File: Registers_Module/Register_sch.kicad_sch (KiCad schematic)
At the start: 22 parts, among them U12 74LS245, U13 74LS173, U14 74LS173

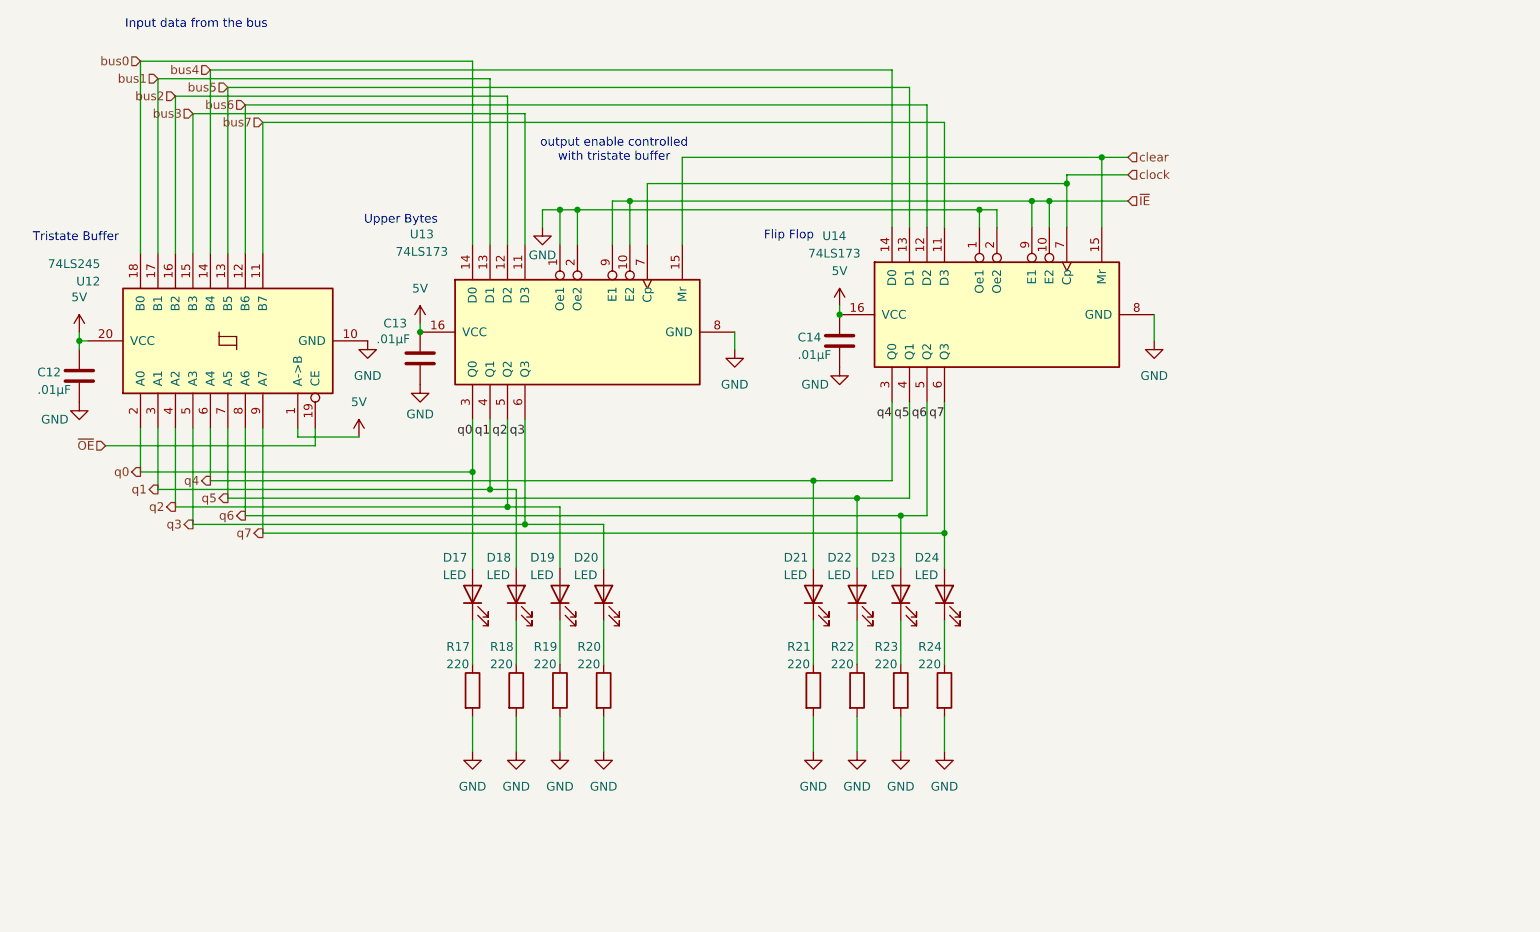
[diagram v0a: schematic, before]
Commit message: updated registers and alu
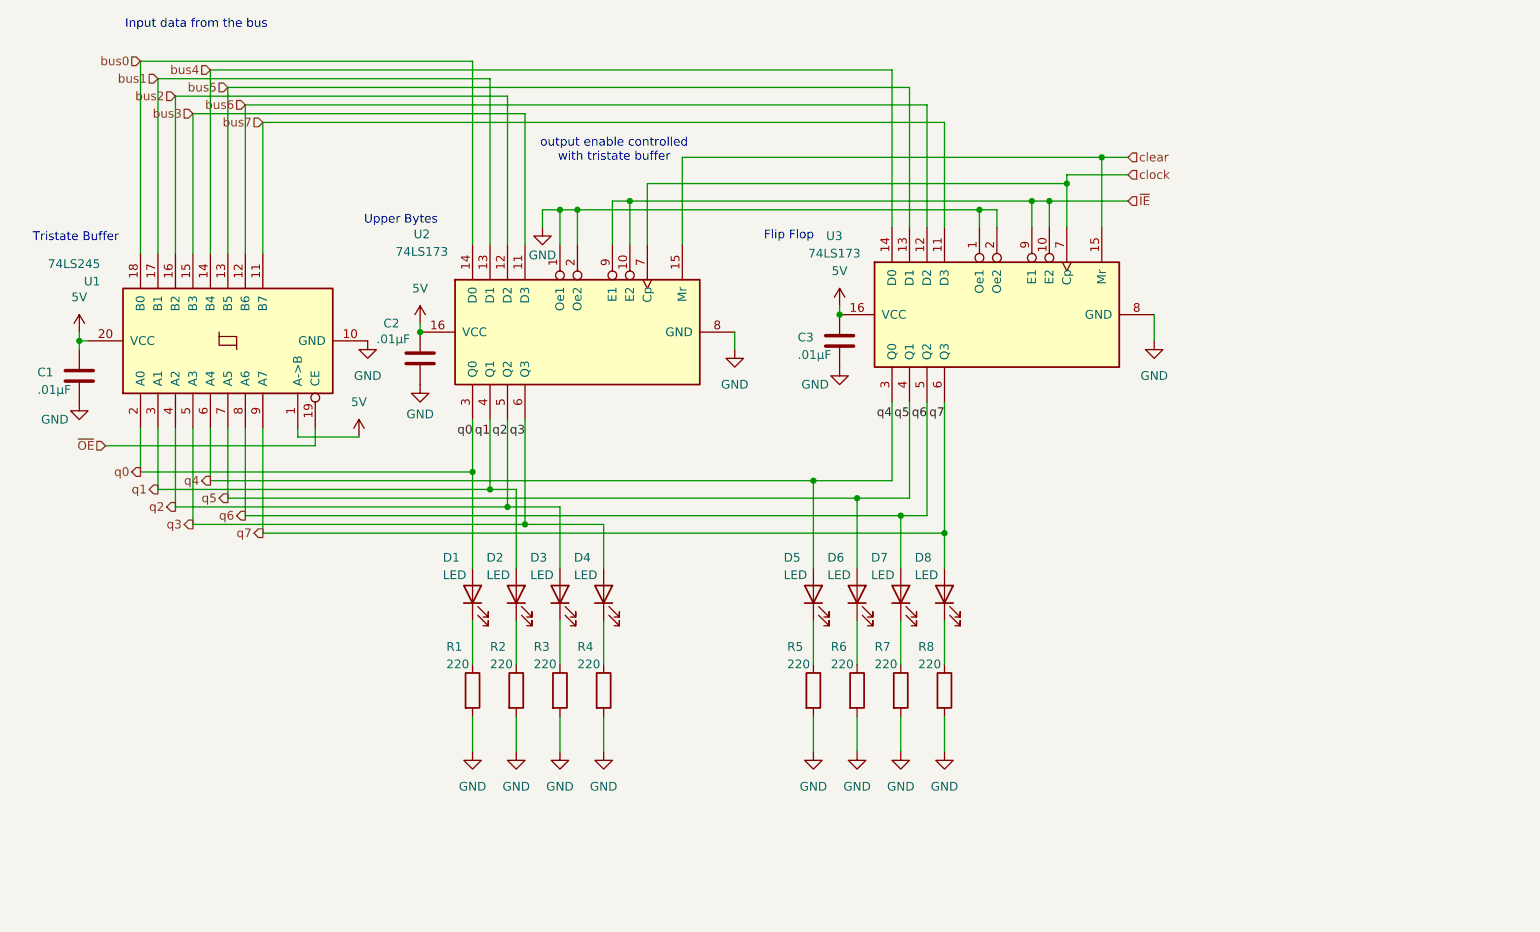
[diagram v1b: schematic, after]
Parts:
- renumbered C12 to C1, C13 to C2, C14 to C3, D17 to D1, D18 to D2, D19 to D3, D20 to D4, D21 to D5, D22 to D6, D23 to D7, D24 to D8, R17 to R1, R18 to R2, R19 to R3, R20 to R4, R21 to R5, R22 to R6, R23 to R7, R24 to R8, U12 to U1, U13 to U2, U14 to U3

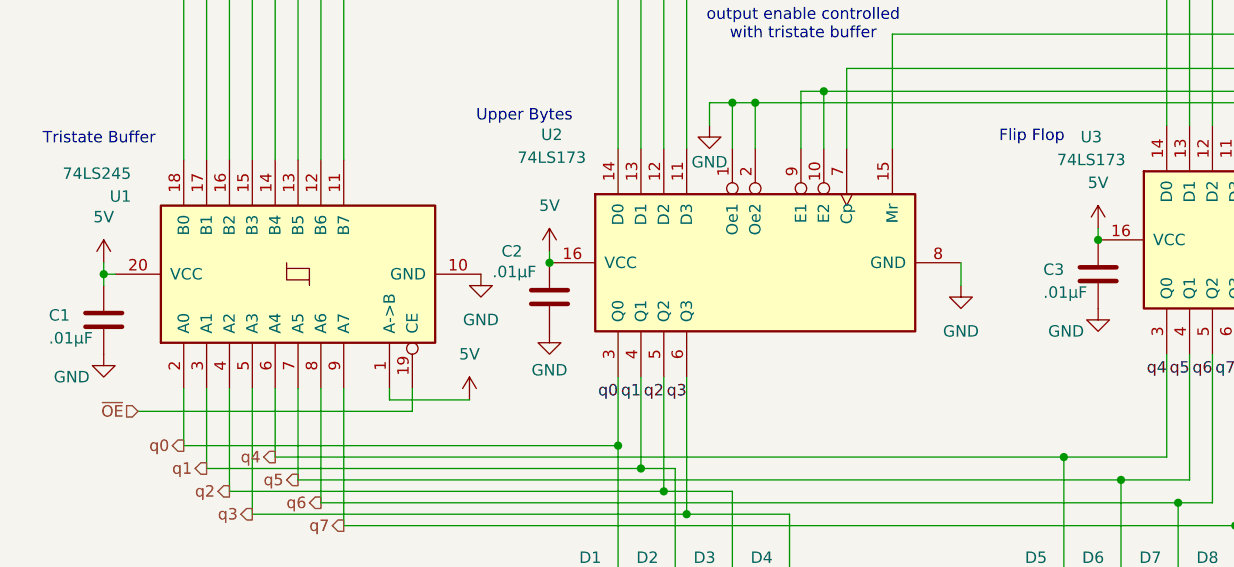
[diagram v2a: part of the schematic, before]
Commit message: added cap's between power pins
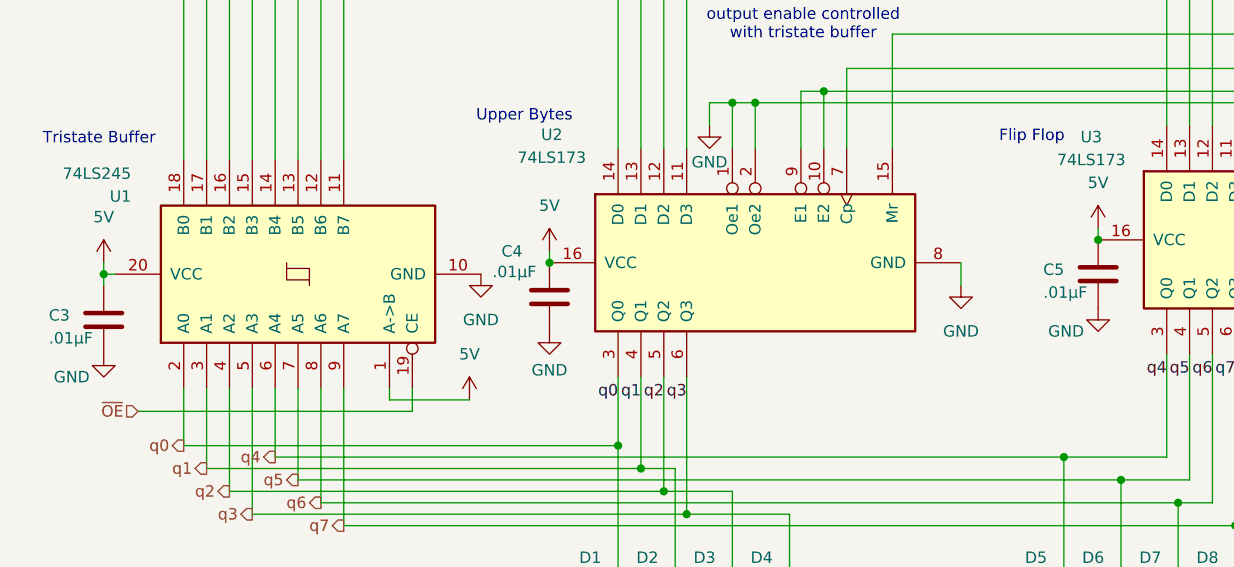
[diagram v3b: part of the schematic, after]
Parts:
- renumbered C1 to C3, C2 to C4, C3 to C5

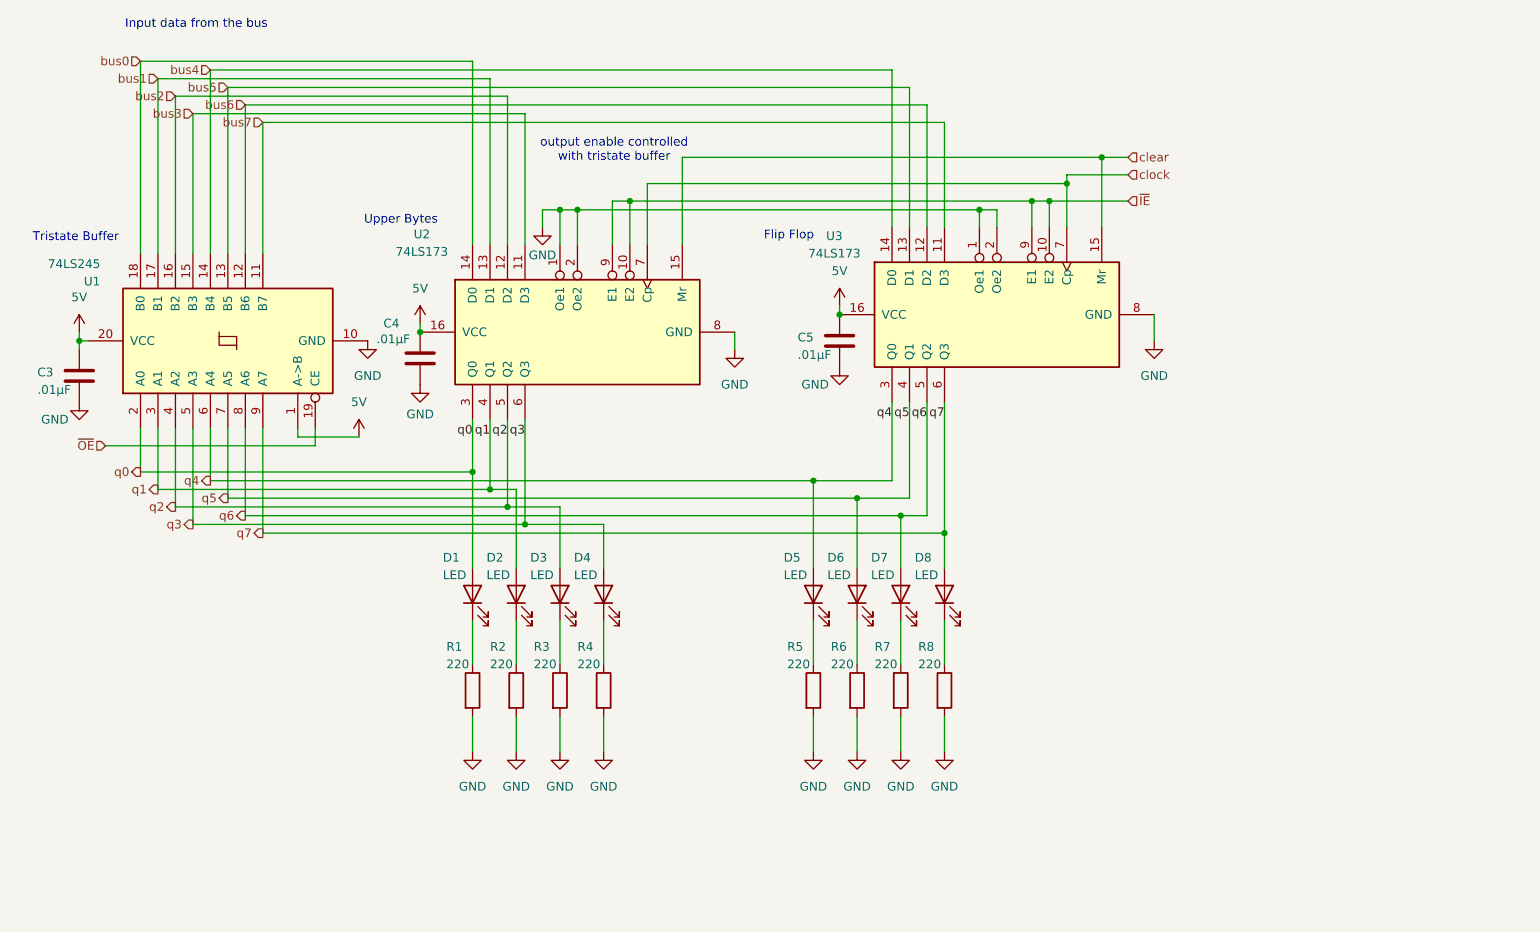
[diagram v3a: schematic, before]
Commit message: updated RAM, changed bus alignment in ALU, RAM, and registers
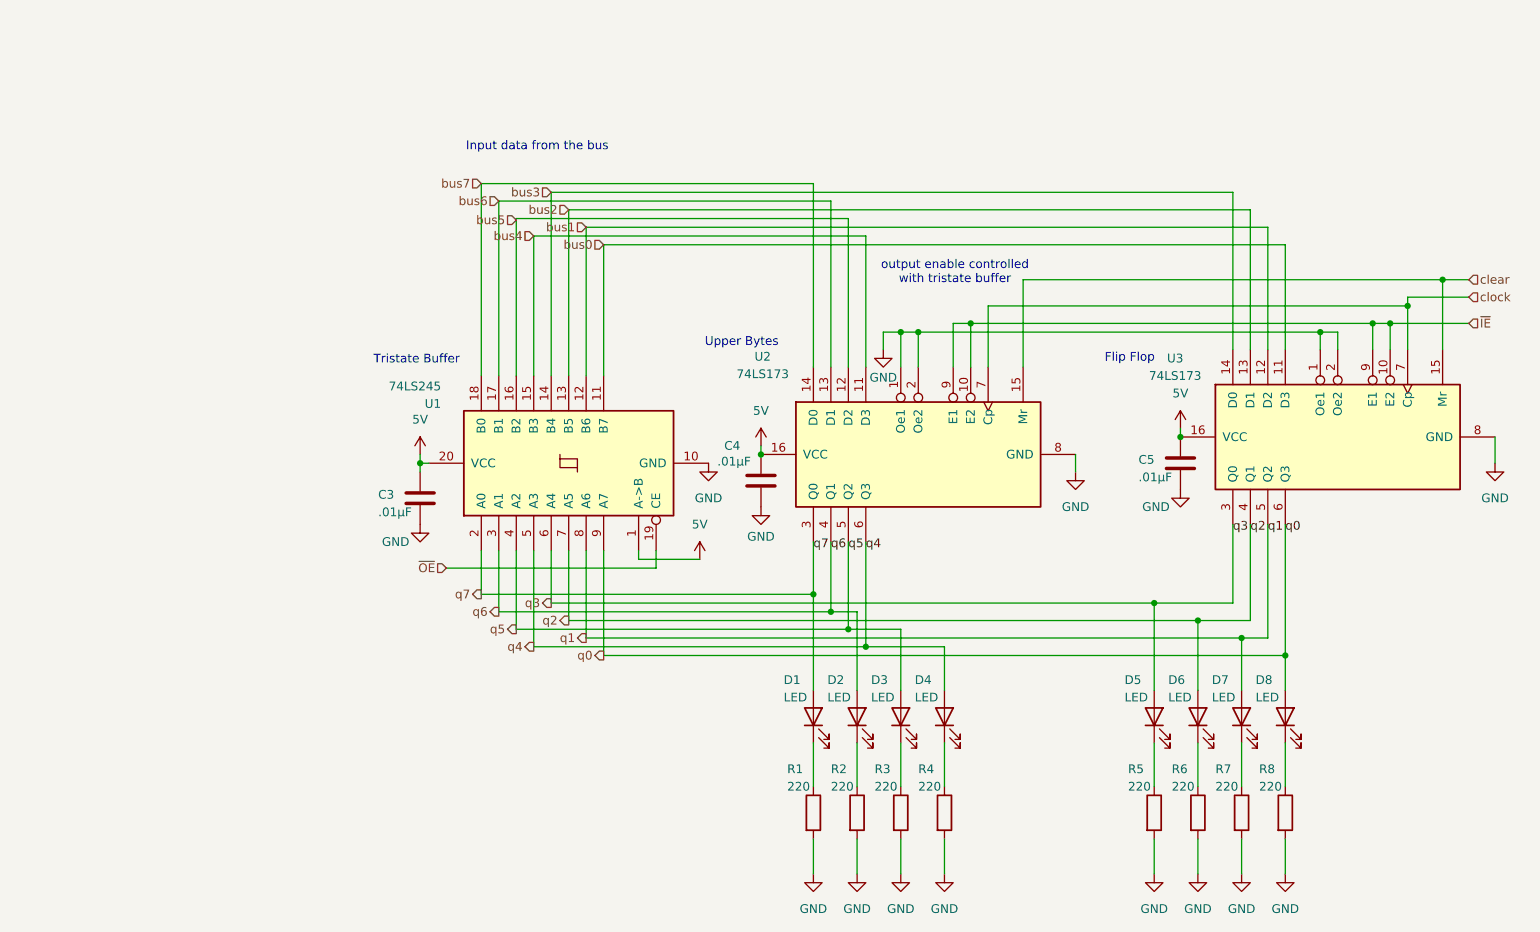
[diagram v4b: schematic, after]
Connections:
- net bus0: now also U1.11 (B7), U3.11 (D3); no longer U1.18 (B0), U2.14 (D0)
- net bus1: now also U1.12 (B6), U3.12 (D2); no longer U1.17 (B1), U2.13 (D1)
- net bus2: now also U1.13 (B5), U3.13 (D1); no longer U1.16 (B2), U2.12 (D2)
- net bus3: now also U1.14 (B4), U3.14 (D0); no longer U1.15 (B3), U2.11 (D3)
- net bus4: now also U1.15 (B3), U2.11 (D3); no longer U1.14 (B4), U3.14 (D0)
- net bus5: now also U1.16 (B2), U2.12 (D2); no longer U1.13 (B5), U3.13 (D1)
- net bus6: now also U1.17 (B1), U2.13 (D1); no longer U1.12 (B6), U3.12 (D2)
- net bus7: now also U1.18 (B0), U2.14 (D0); no longer U1.11 (B7), U3.11 (D3)
- net q0: now also D8.2 (A), U1.9 (A7), U3.6 (Q3); no longer D1.2 (A), U1.2 (A0), U2.3 (Q0)
- net q1: now also D7.2 (A), U1.8 (A6), U3.5 (Q2); no longer D2.2 (A), U1.3 (A1), U2.4 (Q1)
- net q2: now also D6.2 (A), U1.7 (A5), U3.4 (Q1); no longer D3.2 (A), U1.4 (A2), U2.5 (Q2)
- net q3: now also D5.2 (A), U1.6 (A4), U3.3 (Q0); no longer D4.2 (A), U1.5 (A3), U2.6 (Q3)
- net q4: now also D4.2 (A), U1.5 (A3), U2.6 (Q3); no longer D5.2 (A), U1.6 (A4), U3.3 (Q0)
- net q5: now also D3.2 (A), U1.4 (A2), U2.5 (Q2); no longer D6.2 (A), U1.7 (A5), U3.4 (Q1)
- net q6: now also D2.2 (A), U1.3 (A1), U2.4 (Q1); no longer D7.2 (A), U1.8 (A6), U3.5 (Q2)
- net q7: now also D1.2 (A), U1.2 (A0), U2.3 (Q0); no longer D8.2 (A), U1.9 (A7), U3.6 (Q3)
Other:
- moved on the sheet: C3, C4, C5, D1, D2, D3, D4, D5, D6, D7, D8, R1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

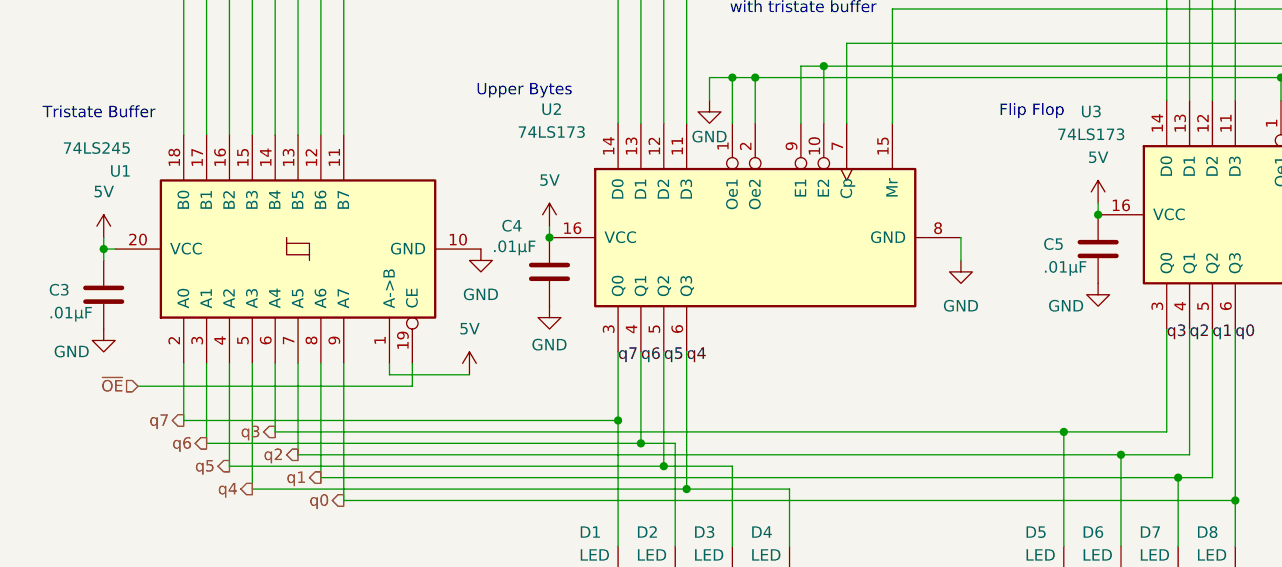
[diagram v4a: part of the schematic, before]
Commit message: fixed Ram register, fixed mar in ram.v, updated caps in alu, ram, and instruction register
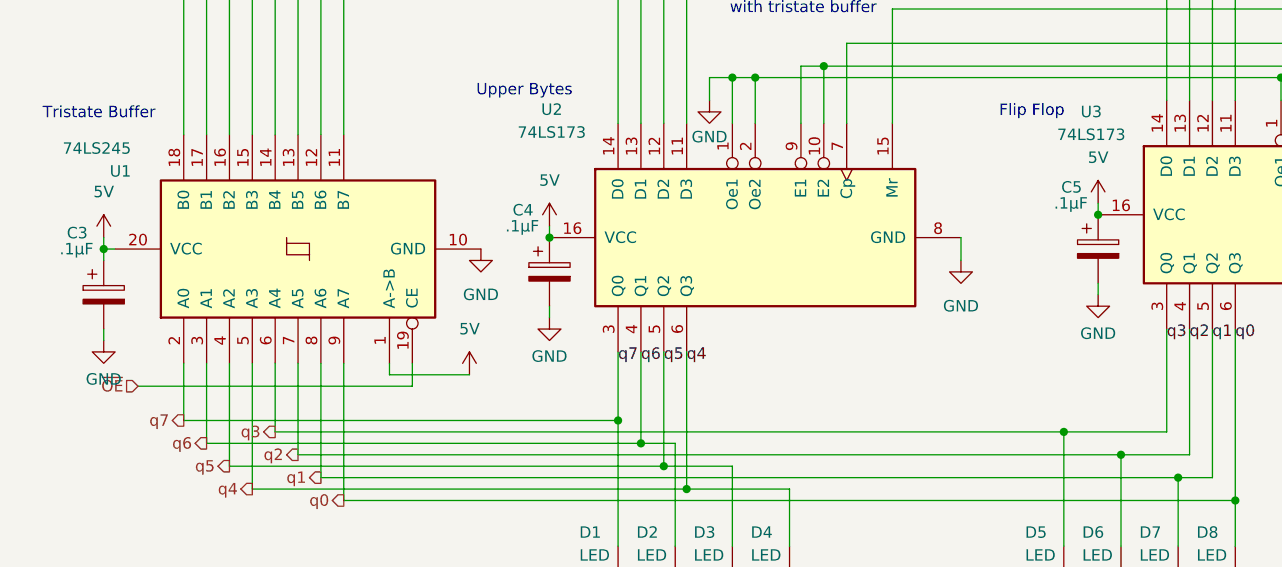
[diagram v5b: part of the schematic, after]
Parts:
- removed C3, C4, C5: .01µF, Capacitor_THT:C_Disc_D5.0mm_W2.5mm_P2.50mm, symbol Device:C
- added C3, C4, C5: .1µF, symbol Device:C_Polarized
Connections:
- net 5V: now also C3.1, C4.1, C5.1
- net GND: now also C3.2, C4.2, C5.2
